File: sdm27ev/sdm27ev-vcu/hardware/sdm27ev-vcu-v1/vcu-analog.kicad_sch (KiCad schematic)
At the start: 90 parts, among them IC15 TPD4E05U06QDQARQ1, IC16 TPD4E05U06QDQARQ1, Q2 TPS2058AD, Q3 TPS2058AD, U4 TCA6408ARSV, U5 TLV9064IRUCR, U6 TLV9064IRUCR, U7 TCA6408ARSV

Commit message: Minor QOL VCU edits before design review
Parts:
- removed R79, R80, R81, R82, R83, R84, R85, R86: 10k, Resistor_SMD:R_0603_1608Metric, symbol Device:R_Small
- added RN3, RN4: 10k, Resistor_SMD:R_Array_Convex_4x0603, symbol Device:R_Pack04
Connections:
- net 3.3V: now also RN3.5 (R4.2), RN3.6 (R3.2), RN3.7 (R2.2), RN3.8 (R1.2), RN4.5 (R4.2), RN4.6 (R3.2), RN4.7 (R2.2), RN4.8 (R1.2)
- net A1_PWR_OC: now also RN4.1 (R1.1)
- net A2_PWR_OC: now also RN4.2 (R2.1)
- net A3_PWR_OC: now also RN4.3 (R3.1)
- net A4_PWR_OC: now also RN4.4 (R4.1)
- net A5_PWR_OC: now also RN3.1 (R1.1)
- net A6_PWR_OC: now also RN3.2 (R2.1)
- net A7_PWR_OC: now also RN3.3 (R3.1)
- net A8_PWR_OC: now also RN3.4 (R4.1)

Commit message: notes from ev vcu design review 10 3
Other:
- note added: "double check math"
- note added: "use 1% or less"
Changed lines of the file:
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@@
+		)
+	)
+	(text "double check math\n"
+		(exclude_from_sim no)
+		(at 182.372 20.066 0)
+		(effects
+			(font
+				(size 1.27 1.27)
+			)
+		)
+	)
+	(text "use 1%\nor less"
+		(exclude_from_sim no)
+		(at 221.234 27.178 0)
+		(effects
+			(font
+				(size 1.27 1.27)
+			)
 		)
 	)

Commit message: VCU updates
Updated P4 Symbol
Digital IO protection rework done
Added pending fixes from design review, e.x SDMC pullups
Needs power review - add this to ToDo
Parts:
- renumbered C37 to C100, C39 to C101, C41 to C102, C45 to C103, C47 to C104, C49 to C105, C51 to C106, C43 to C107, C65 to C68, C66 to C69, C64 to C76, C67 to C77, C61 to C78, C62 to C79, C60 to C80, C63 to C81, C52 to C82, C53 to C83, C54 to C84, C55 to C85, C56 to C86, C57 to C87, C58 to C88, C59 to C89, C42 to C90, C35 to C91, C36 to C92, C38 to C93, C40 to C94, C44 to C95, C46 to C96, C48 to C97, C50 to C98, C34 to C99, IC15 to IC23, IC16 to IC24, Q2 to Q4, Q3 to Q5, R60 to R100, R62 to R101, R64 to R102, R66 to R103, R68 to R125, R70 to R126, R20 to R127, R21 to R128, R22 to R129, R23 to R130, R45 to R131, R46 to R132, R47 to R133, R48 to R134, R49 to R135, R52 to R136, R53 to R137, R54 to R138, R16 to R38, R17 to R40, R18 to R43, R19 to R44, R71 to R81, R72 to R82, R73 to R83, R74 to R84, R75 to R85, R76 to R86, R77 to R88, R78 to R89, R56 to R90, R57 to R91, R59 to R92, R61 to R93, R63 to R94, R65 to R95, R67 to R96, R69 to R97, R55 to R98, R58 to R99, RN4 to RN10, RN3 to RN11, U7 to U16, U5 to U17, U6 to U18, U4 to U9

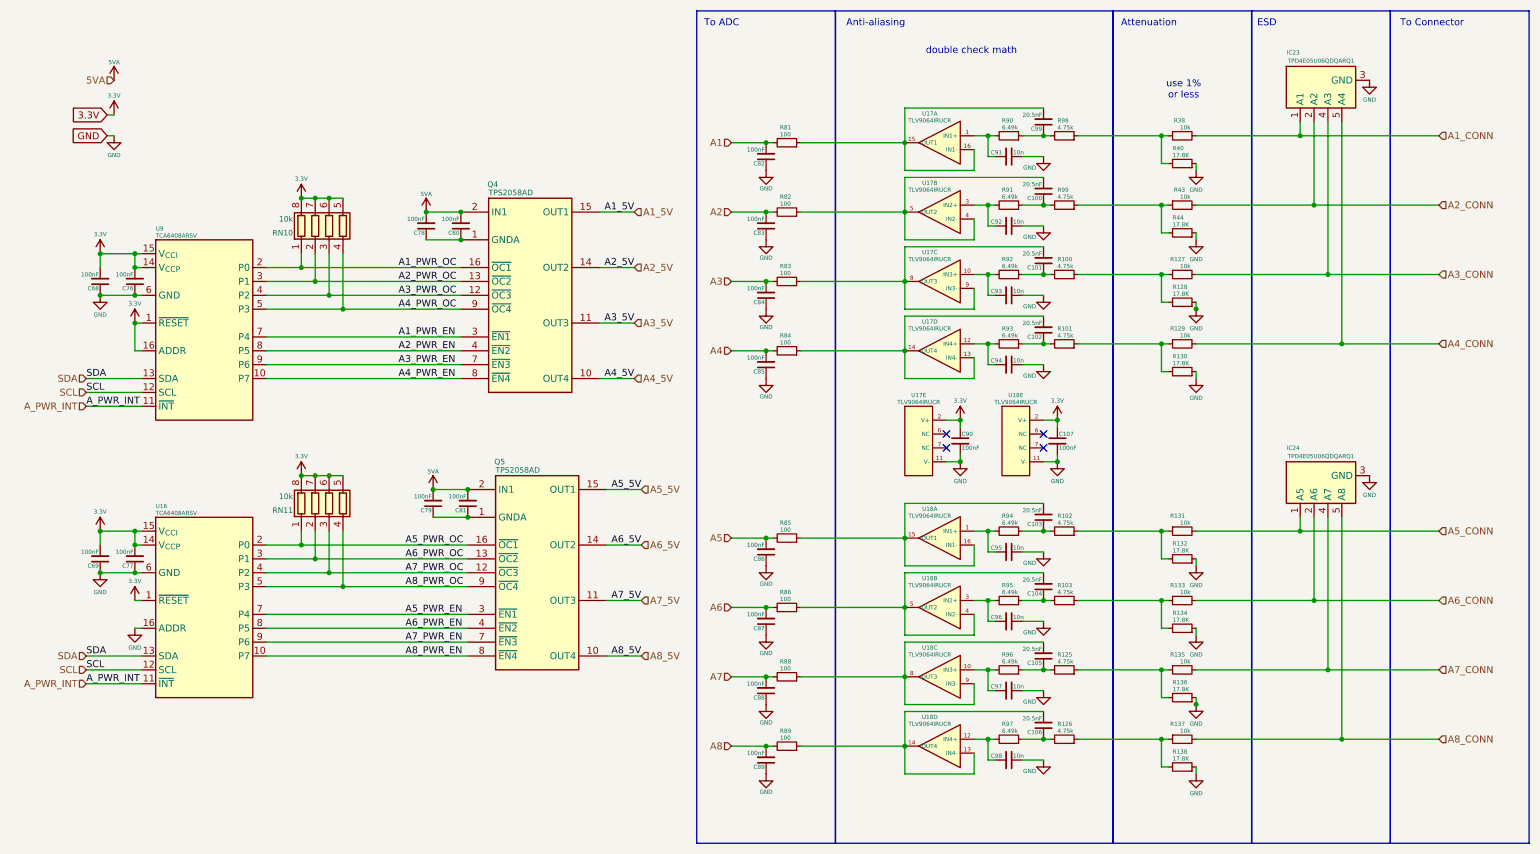
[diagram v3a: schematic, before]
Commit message: VCU sch reorg and power rework
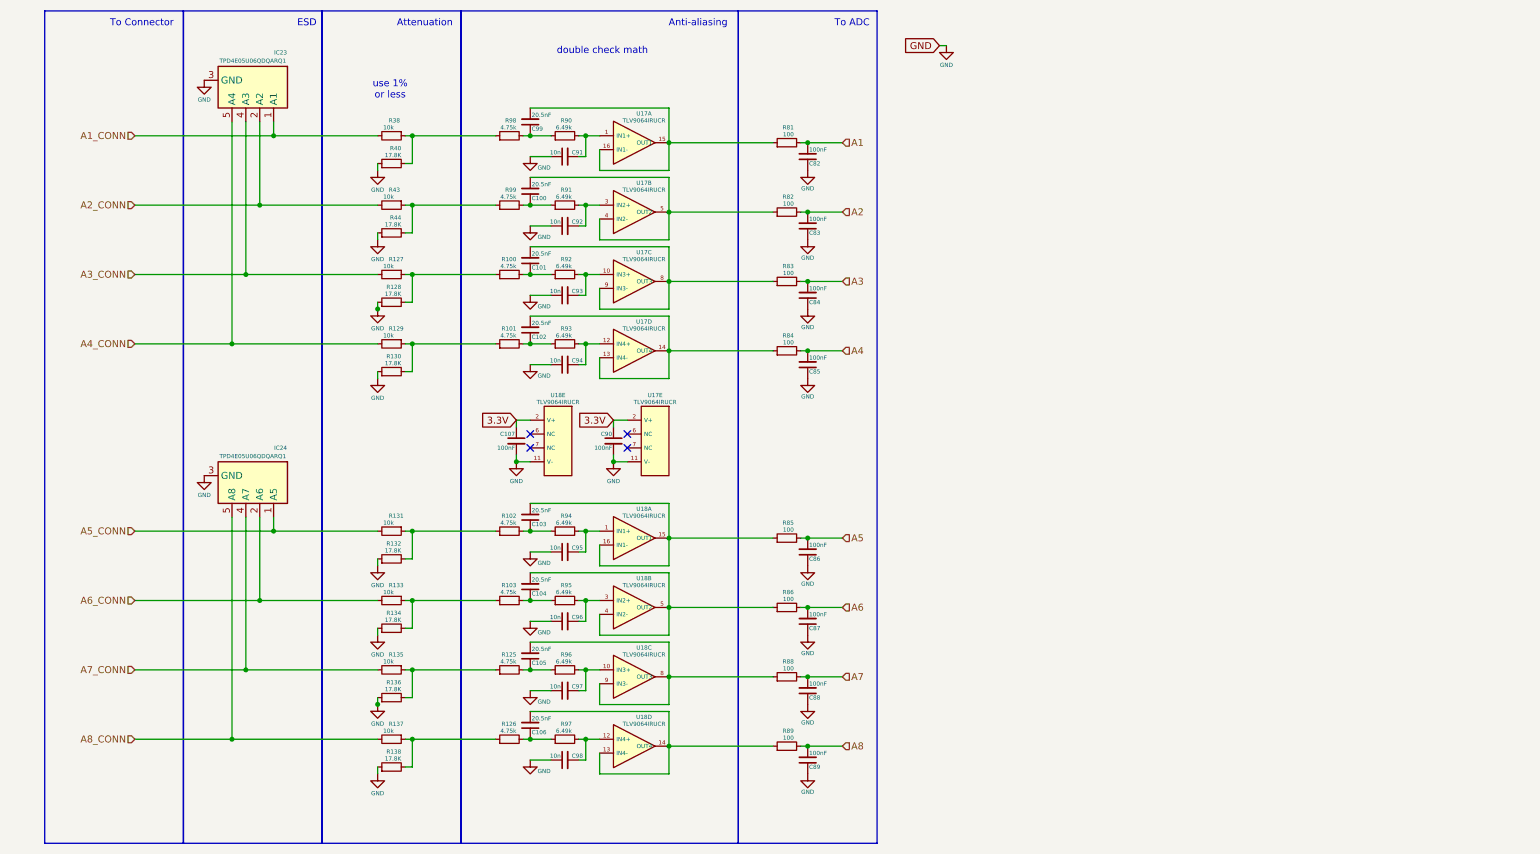
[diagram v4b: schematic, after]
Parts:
- removed C68, C69, C76, C77, C78, C79, C80, C81: 100nF, Capacitor_SMD:C_0603_1608Metric, symbol Device:C_Small
- removed Q4, Q5: TPS2058AD, SOIC127P600X175-16N, symbol SDM_EV:TPS2058AD
- removed RN10, RN11: 10k, Resistor_SMD:R_Array_Convex_4x0603, symbol Device:R_Pack04
- removed U16, U9: TCA6408ARSV, Package_DFN_QFN:UQFN-16_1.8x2.6mm_P0.4mm, symbol Interface_Expansion:TCA6408ARSV
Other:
- moved on the sheet: C100, C101, C102, C103, C104, C105, C106, C107, C82, C83, C84, C85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

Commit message: EV VCU edits, mostly organizational and pre layout/footprint assigned
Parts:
- removed IC23: TPD4E05U06QDQARQ1, DQA(R-PUSON-N10), symbol SDM_EV:TPD4E05U06QDQARQ1
- removed unit 1 of U17
- removed unit 3 of U17
- removed unit 4 of U17
- removed unit 2 of U17
- added D25, D26, D28, D29, D30, D31, D32, D33: PESD24VL1BLS-QYL, SDM_EV:PESD24VL1BLSQYL-Compact, symbol SDM_EV:PESD24VL1BLS-QYL
- added IC7: TLV9064IRUCR, symbol SDM_EV:TLV9064IRUCR
- added U2, U4: TLV9062xDSG, Package_SON:WSON-8-1EP_2x2mm_P0.5mm_EP0.9x1.6mm_ThermalVias, symbol Amplifier_Operational:TLV9062xDSG
- IC24: footprint DQA(R-PUSON-N10) -> (none)
- U17, U18: footprint (none) -> SDM_EV:QFN40P200X200X40-14N
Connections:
- net A1: now also C86.2, R85.2; no longer C82.2, R81.2
- net A1_CONN: now also D25.1
- net A2: now also C87.2, R86.2; no longer C83.2, R82.2
- net A2_CONN: now also D26.1
- net A3: now also C88.2, R88.2; no longer C84.2, R83.2
- net A3_CONN: now also D28.1
- net A4: now also C89.2, R89.2; no longer C85.2, R84.2
- net A4_CONN: now also D29.1
- net A5: now also C82.2, R81.2; no longer C86.2, R85.2
- net A5_CONN: now also D30.1
- net A6: now also C83.2, R82.2; no longer C87.2, R86.2
- net A6_CONN: now also D31.1
- net A7: now also C84.2, R83.2; no longer C88.2, R88.2
- net A7_CONN: now also D32.1
- net A8: now also C85.2, R84.2; no longer C89.2, R89.2
- net A8_CONN: now also D33.1
- net GND: now also U17.10 (V-), U18.10 (V-), D25.2, D26.2, D28.2, D29.2, D30.2, D31.2, D32.2, D33.2, U2.4 (V-), U2.9 (PAD), U4.4 (V-), U4.9 (PAD); no longer U17.11 (V-), U18.11 (V-)
- net at C102.2, R84.1: now also U4.6 (-), U4.7
- net at C101.2, R83.1: now also U4.1, U4.2 (-)
- net at C92.2, R91.2: now also U2.5 (+)
- net at C99.2, R81.1: now also U2.1, U2.2 (-)
- net at C94.2, R93.2: now also U4.5 (+)
- net at C91.2, R90.2: now also U2.3 (+)
- net at C93.2, R92.2: now also U4.3 (+)
- net at C106.2, R89.1, U18.13 (OUT4): now also U18.12 (IN4-); no longer U18.14 (OUT4)
- net at C98.2, R97.2: now also U18.11 (IN4+); no longer U18.12 (IN4+)
- net at C103.2, R85.1: now also U18.14 (OUT1), U18.2 (IN1-); no longer U18.15 (OUT1), U18.16 (IN1-)
- net at C96.2, R95.2: now also U18.4 (IN2+); no longer U18.3 (IN2+)
- net at C97.2, R96.2: now also U18.9 (IN3+); no longer U18.10 (IN3+)
- net at C105.2, R88.1, U18.8 (IN3-): now also U18.7 (OUT3); no longer U18.9 (IN3-)
- net at C104.2, R86.1, U18.5 (IN2-): now also U18.6 (OUT2); no longer U18.4 (IN2-)
- net at C100.2, R82.1: now also U2.6 (-), U2.7
- net 3.3V renamed A3.3V
- net A3.3V: now also U17.3 (V+), U18.3 (V+), U2.8 (V+), U4.8 (V+); no longer U17.2 (V+), U18.2 (V+)
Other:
- moved on the sheet: C102, C90
